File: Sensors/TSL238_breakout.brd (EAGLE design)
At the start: 100 x 80 mm, 1 part

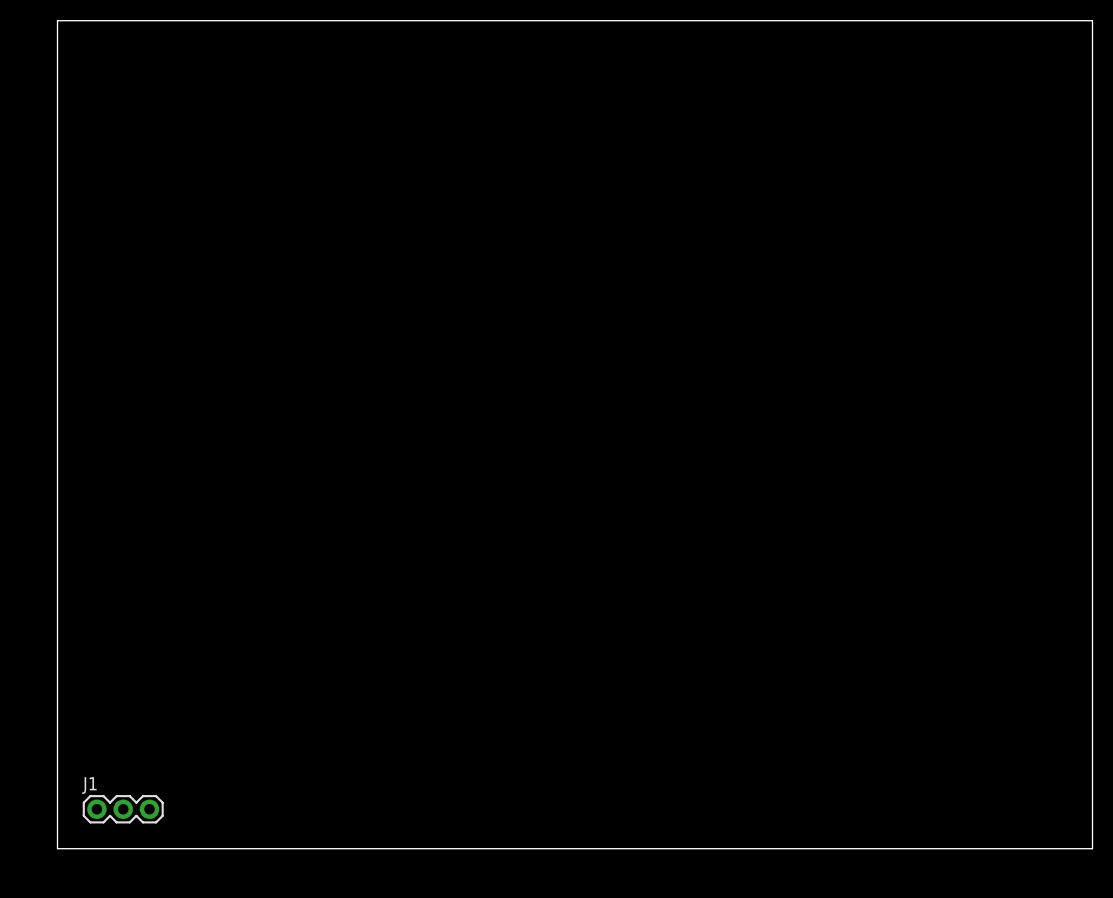
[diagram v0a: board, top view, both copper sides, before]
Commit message: Updated TSL238
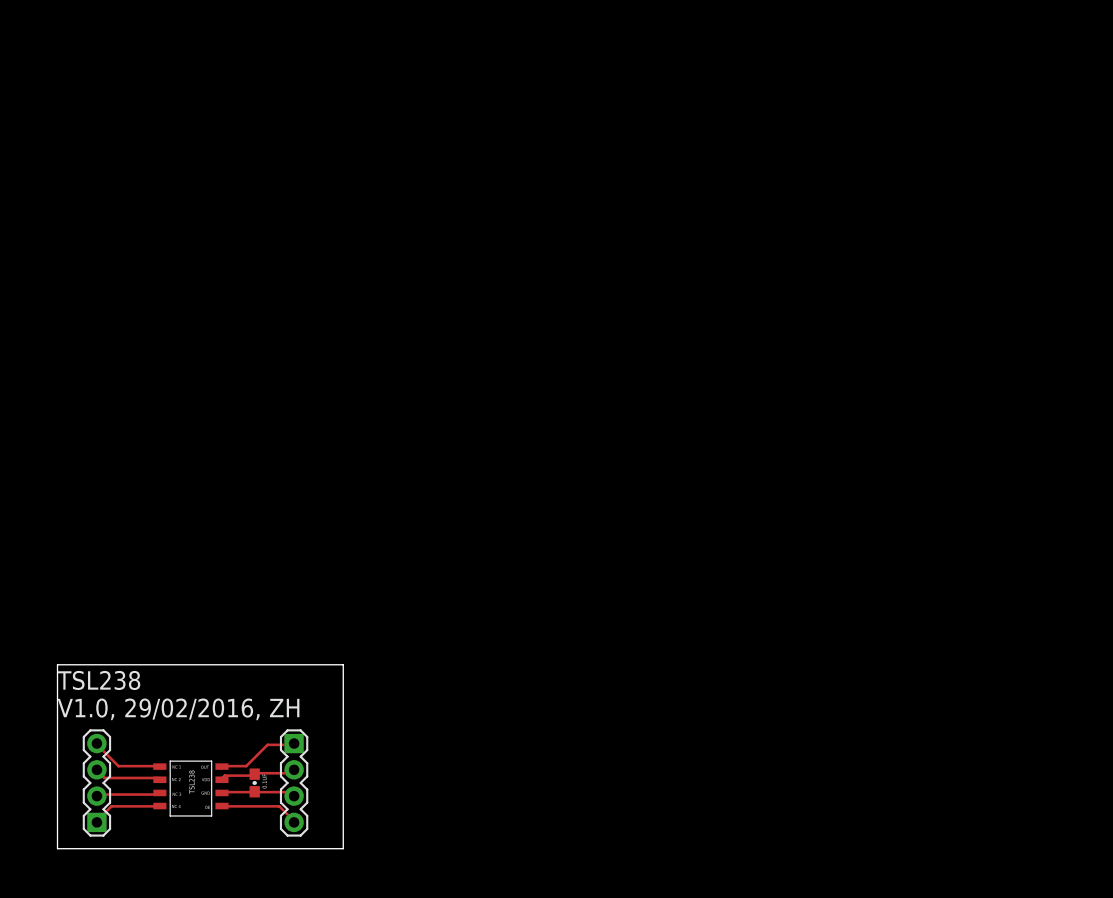
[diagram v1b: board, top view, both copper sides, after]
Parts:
- added 0.1UF: (no value), SparkFun-Capacitors:0603-CAP
- added J2: (no value), SparkFun-Connectors:1X04
- added U$1: TSL238, awqua_eagle_library:TSL238
- J1: device SparkFun-Connectors:1X03 -> SparkFun-Connectors:1X04
- moved J1 20.1 mm to (22.9, 10.2), turned to 270 degrees
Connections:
- new net N$1: J2.1, U$1.NC4
- new net N$2: J2.2, U$1.NC3
- new net N$3: J2.3, U$1.NC2
- new net N$4: J2.4, U$1.NC1
- new net N$5: J1.4, U$1.OE
- new net N$6: 0.1UF.1, J1.2, U$1.VDD
- new net N$8: J1.1, U$1.OUT
- new net N$9: 0.1UF.2, J1.3, U$1.GND
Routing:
- net N$8: track 0.00 -> 7.92 mm
- net N$5: track 0.00 -> 7.68 mm
- net N$6: track 0.00 -> 7.44 mm
- net N$9: track 0.00 -> 7.22 mm
- net N$4: track 0.00 -> 7.05 mm
- net N$1: track 0.00 -> 6.81 mm
- net N$3: track 0.00 -> 6.54 mm
- net N$2: track 0.00 -> 6.29 mm
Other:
- board size 100 x 80 mm -> 27.6 x 17.8 mm
- board text added: "TSL238 V1.0, 29/02/2016, ZH"
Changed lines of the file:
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@@
 <layer number="111" name="LPC17xx" color="7" fill="1" visible="yes" active="yes"/>
 <layer number="112" name="tSilk" color="7" fill="1" visible="yes" active="yes"/>
-<layer number="113" name="IDFDebug" color="4" fill="1" visible="yes" active="yes"/>
+<layer number="113" name="IDFDebug" color="7" fill="1" visible="yes" active="yes"/>
 <layer number="114" name="Badge_Outline" color="7" fill="1" visible="yes" active="yes"/>
 <layer number="115" name="ReferenceISLANDS" color="7" fill="1" visible="yes" active="yes"/>
@@
 <board>
 <plain>
-<wire x1="0" y1="0" x2="100" y2="0" width="0" layer="20"/>
-<wire x1="100" y1="0" x2="100" y2="80" width="0" layer="20"/>
-<wire x1="100" y1="80" x2="0" y2="80" width="0" layer="20"/>
-<wire x1="0" y1="80" x2="0" y2="0" width="0" layer="20"/>
+<wire x1="0" y1="0" x2="27.61" y2="0" width="0" layer="20"/>
+<wire x1="27.61" y1="0" x2="27.61" y2="17.77" width="0" layer="20"/>
+<wire x1="27.61" y1="17.77" x2="0" y2="17.77" width="0" layer="20"/>
+<wire x1="0" y1="17.77" x2="0" y2="0" width="0" layer="20"/>
+<text x="0" y="12.7" size="1.778" layer="21">TSL238
+V1.0, 29/02/2016, ZH</text>
 </plain>
 <attributes>
@@
 <autorouter>
 <pass name="Default">
-<param name="RoutingGrid" value="50mil"/>
+<param name="RoutingGrid" value="12.5mil"/>
 <param name="AutoGrid" value="1"/>
 <param name="Efforts" value="0"/>
 <param name="TopRouterVariant" value="1"/>
 <param name="tpViaShape" value="round"/>
-<param name="PrefDir.1" value="a"/>
+<param name="PrefDir.1" value="-"/>
 <param name="PrefDir.2" value="0"/>
 <param name="PrefDir.3" value="0"/>
@@
 <param name="PrefDir.14" value="0"/>
 <param name="PrefDir.15" value="0"/>
-<param name="PrefDir.16" value="a"/>
+<param name="PrefDir.16" value="|"/>
 <param name="cfVia" value="8"/>
 <param name="cfNonPref" value="5"/>
@@
 </autorouter>
 <elements>
-<element name="J1" library="SparkFun-Connectors" package="1X03" value="" x="3.81" y="3.81"/>
+<element name="0.1UF" library="SparkFun-Capacitors" package="0603-CAP" value="" x="19.05" y="6.35" rot="R270"/>
+<element name="J1" library="SparkFun-Connectors" package="1X04" value="" x="22.86" y="10.16" smashed="yes" rot="R270">
+<attribute name="PROD_ID" value="CONN-09696" x="22.86" y="10.16" size="1.778" layer="27" rot="R270" display="off"/>
+<attribute name="VALUE" x="19.685" y="11.43" size="1.27" layer="27" rot="R270"/>
+</element>
+<element name="J2" library="SparkFun-Connectors" package="1X04" value="" x="3.81" y="2.54" smashed="yes" rot="R90">
+<attribute name="PROD_ID" value="CONN-09696" x="3.81" y="2.54" size="1.778" layer="27" rot="R90" display="off"/>
+<attribute name="VALUE" x="6.985" y="1.27" size="1.27" layer="27" rot="R90"/>
+</element>
+<element name="U$1" library="awqua_eagle_library" package="TSL238" value="TSL238" x="12.7" y="7.62" rot="R270"/>
 </elements>
 <signals>
+<signal name="N$1">
+<contactref element="U$1" pad="NC4"/>
+<contactref element="J2" pad="1"/>
+<wire x1="5.207" y1="4.0894" x2="9.779" y2="4.0894" width="0.254" layer="1"/>
+<wire x1="3.8354" y1="2.7178" x2="5.207" y2="4.0894" width="0.254" layer="1"/>
+<wire x1="9.779" y1="4.0894" x2="9.89" y2="4.12" width="0.254" layer="1"/>
+<wire x1="3.8354" y1="2.7178" x2="3.81" y2="2.54" width="0.254" layer="1"/>
+</signal>
+<signal name="N$2">
+<contactref element="U$1" pad="NC3"/>
+<contactref element="J2" pad="2"/>
+<wire x1="3.8354" y1="5.2324" x2="9.779" y2="5.2324" width="0.254" layer="1"/>
+<wire x1="9.779" y1="5.2324" x2="9.89" y2="5.39" width="0.254" layer="1"/>
+<wire x1="3.8354" y1="5.2324" x2="3.81" y2="5.08" width="0.254" layer="1"/>
+</signal>
+<signal name="N$3">
+<contactref element="U$1" pad="NC2"/>
+<contactref element="J2" pad="3"/>
+<wire x1="4.5212" y1="6.8326" x2="9.779" y2="6.8326" width="0.254" layer="1"/>
+<wire x1="3.8354" y1="7.5184" x2="4.5212" y2="6.8326" width="0.254" layer="1"/>
+<wire x1="9.779" y1="6.8326" x2="9.89" y2="6.66" width="0.254" layer="1"/>
+<wire x1="3.8354" y1="7.5184" x2="3.81" y2="7.62" width="0.254" layer="1"/>
+</signal>
+<signal name="N$4">
+<contactref element="U$1" pad="NC1"/>
+<contactref element="J2" pad="4"/>
+<wire x1="5.8928" y1="7.9756" x2="9.779" y2="7.9756" width="0.254" layer="1"/>
+<wire x1="3.8354" y1="10.033" x2="5.8928" y2="7.9756" width="0.254" layer="1"/>
+<wire x1="9.779" y1="7.9756" x2="9.89" y2="7.93" width="0.254" layer="1"/>
+<wire x1="3.8354" y1="10.033" x2="3.81" y2="10.16" width="0.254" layer="1"/>
+</signal>
+<signal name="N$5">
+<contactref element="U$1" pad="OE"/>
+<contactref element="J1" pad="4"/>
+<wire x1="21.4376" y1="4.0894" x2="15.9512" y2="4.0894" width="0.254" layer="1"/>
+<wire x1="22.8092" y1="2.7178" x2="21.4376" y2="4.0894" width="0.254" layer="1"/>
+<wire x1="15.9512" y1="4.0894" x2="15.89" y2="4.12" width="0.254" layer="1"/>
+<wire x1="22.8092" y1="2.7178" x2="22.86" y2="2.54" width="0.254" layer="1"/>
+</signal>
+<signal name="N$8">
+<contactref element="U$1" pad="OUT"/>
+<contactref element="J1" pad="1"/>
+<wire x1="18.2372" y1="7.9756" x2="15.9512" y2="7.9756" width="0.254" layer="1"/>
+<wire x1="20.2946" y1="10.033" x2="18.2372" y2="7.9756" width="0.254" layer="1"/>
+<wire x1="22.8092" y1="10.033" x2="20.2946" y2="10.033" width="0.254" layer="1"/>
+<wire x1="15.9512" y1="7.9756" x2="15.89" y2="7.93" width="0.254" layer="1"/>
+<wire x1="22.8092" y1="10.033" x2="22.86" y2="10.16" width="0.254" layer="1"/>
+</signal>
+<signal name="N$9">
+<contactref element="J1" pad="3"/>
+<contactref element="U$1" pad="GND"/>
+<contactref element="0.1UF" pad="2"/>
+<wire x1="15.9512" y1="5.461" x2="18.923" y2="5.461" width="0.254" layer="1"/>
+<wire x1="18.923" y1="5.461" x2="19.05" y2="5.5" width="0.254" layer="1"/>
+<wire x1="15.9512" y1="5.461" x2="15.89" y2="5.39" width="0.254" layer="1"/>
+<wire x1="22.5806" y1="5.461" x2="19.1516" y2="5.461" width="0.254" layer="1"/>
+<wire x1="22.8092" y1="5.2324" x2="22.5806" y2="5.461" width="0.254" layer="1"/>
+<wire x1="19.1516" y1="5.461" x2="19.05" y2="5.5" width="0.254" layer="1"/>
+<wire x1="22.8092" y1="5.2324" x2="22.86" y2="5.08" width="0.254" layer="1"/>
+</signal>
+<signal name="N$6">
+<contactref element="J1" pad="2"/>
+<contactref element="U$1" pad="VDD"/>
+<contactref element="0.1UF" pad="1"/>
+<wire x1="16.1798" y1="7.0612" x2="18.923" y2="7.0612" width="0.254" layer="1"/>
+<wire x1="15.9512" y1="6.8326" x2="16.1798" y2="7.0612" width="0.254" layer="1"/>
+<wire x1="18.923" y1="7.0612" x2="19.05" y2="7.2" width="0.254" layer="1"/>
+<wire x1="15.9512" y1="6.8326" x2="15.89" y2="6.66" width="0.254" layer="1"/>
+<wire x1="22.5806" y1="7.2898" x2="19.1516" y2="7.2898" width="0.254" layer="1"/>
+<wire x1="22.8092" y1="7.5184" x2="22.5806" y2="7.2898" width="0.254" layer="1"/>
+<wire x1="19.1516" y1="7.2898" x2="19.05" y2="7.2" width="0.254" layer="1"/>
+<wire x1="22.8092" y1="7.5184" x2="22.86" y2="7.62" width="0.254" layer="1"/>
+</signal>
 </signals>
 </board>
 </drawing>
+<compatibility>
+<note version="6.3" minversion="6.2.2" severity="warning">
+Since Version 6.2.2 text objects can contain more than one line,
+which will not be processed correctly with this version.
+</note>
+</compatibility>
 </eagle>

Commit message: updated tsl238
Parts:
- removed J2: (no value), SparkFun-Connectors:1X04
- moved 0.1UF 9.98 mm to (9.40, 3.81)
- moved J1 9.94 mm to (13.0, 9.40)
- moved U$1 8.76 mm to (4.32, 5.08)
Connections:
- net N$5 renamed OE
- net N$6 renamed VCC
- net N$8 renamed OUT
- net N$9 renamed GND
- removed net N$1: J2.1, U$1.NC4
- removed net N$2: J2.2, U$1.NC3
- removed net N$3: J2.3, U$1.NC2
- removed net N$4: J2.4, U$1.NC1
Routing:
- net N$4: track 7.05 -> 0.00 mm
- net N$1: track 6.81 -> 0.00 mm
- net N$3: track 6.54 -> 0.00 mm
- net N$2: track 6.29 -> 0.00 mm
- net OE: track 7.68 -> 5.53 mm
- net GND: track 7.22 -> 6.02 mm
- net VCC: track 7.44 -> 6.72 mm
- added copper zone on layer 16, net GND
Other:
- board size 27.6 x 17.8 mm -> 14.2 x 11.2 mm
- board text added: "GND"
- board text added: "OE"
- board text added: "OUT"
- board text added: "TSL238 Breakout Board"
- board text added: "VCC"
- board text removed: "TSL238 V1.0, 29/02/2016, ZH"
